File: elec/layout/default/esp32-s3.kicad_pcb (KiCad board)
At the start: 2 copper layers, 66.4 x 94.6 mm, 6 parts

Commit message: added layout
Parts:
- C1: value 100.0 nF -> Multilayer Ceramic Capacitors MLCC - SMD/SMT 100nF 10V 0402 RoHS
- C2, C3: value 10.0 uF -> Multilayer Ceramic Capacitors MLCC - SMD/SMT 10uF 10V 0805 RoHS
- R1: value 8.2 KΩ -> Chip Resistor - Surface Mount 11KOhms ±5% 1/16W 0402 RoHS
- moved C1 72.3 mm to (103.9, 82.7), turned to 90 degrees
- moved C2 71.2 mm to (102.4, 82.6), turned to 90 degrees
- moved R1 69.4 mm to (103.3, 85.4), turned to -90 degrees
- moved C3 68.7 mm to (100.4, 82.6), turned to 90 degrees
- moved U2 64.0 mm to (101.1, 87.4), turned to -90 degrees
- moved U1 45.9 mm to (114.4, 90.9)
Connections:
- net EN renamed en
- net IO0 renamed io0
- net IO1 renamed io1
- net IO10 renamed io10
- net IO11 renamed io11
- net IO12 renamed io12
- net IO13 renamed io13
- net IO14 renamed io14
- net IO15 renamed io15
- net IO16 renamed io16
- net IO17 renamed io17
- net IO18 renamed io18
- net IO2 renamed io2
- net IO21 renamed io21
- net IO3 renamed io3
- net IO35 renamed io35
- net IO36 renamed io36
- net IO37 renamed io37
- net IO38 renamed io38
- net IO4 renamed io4
- net IO45 renamed io45
- net IO46 renamed io46
- net IO47 renamed io47
- net IO48 renamed io48
- net IO5 renamed io5
- net IO6 renamed io6
- net IO7 renamed io7
- net IO8 renamed io8
- net IO9 renamed io9
- net RXD0 renamed rxd0
- net TXD0 renamed txd0
- net dm renamed io19
- net dp renamed io20
- net tck renamed io39
- net tdi renamed io41
- net tdo renamed io40
- net tms renamed io42
- C1 pad 1: vcc-1 -> vcc
- C1 pad 2: gnd-1 -> gnd
- C2 pad 1: vcc-2 -> vcc
- C2 pad 2: gnd-2 -> gnd
- C3 pad 1: vcc-3 -> vcc
- C3 pad 2: gnd-3 -> gnd
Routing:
- net en: track 0.00 -> 8.40 mm
- net vcc: track 0.00 -> 7.15 mm
- net gnd: track 0.00 -> 5.54 mm

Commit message: layout updates
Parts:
- C1: value Multilayer Ceramic Capacitors MLCC - SMD/SMT 100nF 10V 0402 RoHS -> 16V 100nF X7R ±10% 0402 Multilayer Ceramic Capacitors MLCC - SMD/SMT ROHS
- C2, C3: value Multilayer Ceramic Capacitors MLCC - SMD/SMT 10uF 10V 0805 RoHS -> 25V 10uF X5R ±10% 0805 Multilayer Ceramic Capacitors MLCC - SMD/SMT ROHS
- R1: value Chip Resistor - Surface Mount 11KOhms ±5% 1/16W 0402 RoHS -> 62.5mW Thick Film Resistors ±100ppm/℃ ±1% 10kΩ 0402 Chip Resistor - Surface Mount ROHS
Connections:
- net gnd renamed ic-gnd
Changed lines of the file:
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@@
   (net 30 "io39")
   (net 31 "io40")
-  (net 32 "gnd")
+  (net 32 "ic-gnd")
   (net 33 "vcc")
   (net 34 "io41")
@@
         (effects (font (size 1 1) (thickness 0.15)))
     )
-    (fp_text value "Multilayer Ceramic Capacitors MLCC - SMD/SMT 100nF 10V 0402 RoHS" (at 0 1.16 90) (layer "F.Fab")
+    (fp_text value "16V 100nF X7R ±10% 0402  Multilayer Ceramic Capacitors MLCC - SMD/SMT ROHS" (at 0 1.16 90) (layer "F.Fab")
         (effects (font (size 1 1) (thickness 0.15)))
     )
@@
       (net 33 "vcc") (pintype "stereo"))
     (pad "2" smd roundrect (at 0.48 0 90) (size 0.56 0.62) (layers "F.Cu" "F.Paste" "F.Mask") (roundrect_rratio 0.25)
-      (net 32 "gnd") (pintype "stereo"))
+      (net 32 "ic-gnd") (pintype "stereo"))
     (model "${KICAD6_3DMODEL_DIR}/Capacitor_SMD.3dshapes/C_0402_1005Metric.wrl"
       (offset (xyz 0 0 0))
@@
         (effects (font (size 1 1) (thickness 0.15)))
     )
-    (fp_text value "Multilayer Ceramic Capacitors MLCC - SMD/SMT 10uF 10V 0805 RoHS" (at 0 1.68 90) (layer "F.Fab")
+    (fp_text value "25V 10uF X5R ±10% 0805  Multilayer Ceramic Capacitors MLCC - SMD/SMT ROHS" (at 0 1.68 90) (layer "F.Fab")
         (effects (font (size 1 1) (thickness 0.15)))
     )
@@
       (net 33 "vcc") (pintype "stereo"))
     (pad "2" smd roundrect (at 0.95 0 90) (size 1 1.45) (layers "F.Cu" "F.Paste" "F.Mask") (roundrect_rratio 0.25)
-      (net 32 "gnd") (pintype "stereo"))
+      (net 32 "ic-gnd") (pintype "stereo"))
     (model "${KICAD6_3DMODEL_DIR}/Capacitor_SMD.3dshapes/C_0805_2012Metric.wrl"
       (offset (xyz 0 0 0))
-      (scale (xyz 1 1 1))
-      (rotate (xyz 0 0 0))
-    )
-  )
-  (footprint "lib:KEY-SMD_4P-L4.2-W3.2-P2.20-LS4.6" (layer "F.Cu")
-    (at 101.112894 87.388566 -90)
-    (attr smd)
-    (fp_text reference "U2" (at 1.943223 -2.508599 90) (layer "F.SilkS")
-        (effects (font (size 1 1) (thickness 0.15)))
-    )
-    (fp_text value "" (at 0 5.07 90) (layer "F.Fab")
-        (effects (font (size 1 1) (thickness 0.15)))
-    )
-    (fp_text user "${REFERENCE}" (at 0 0 90) (layer "F.Fab")
-        (effects (font (size 1 1) (thickness 0.15)))
-    )
-    (fp_line (start -2.2 -0.54) (end -2.2 0.54)
-      (stroke (width 0.25) (type solid)) (layer "F.SilkS"))
-    (fp_line (start -1.38 1.55) (end 1.38 1.55)
-      (stroke (width 0.25) (type solid)) (layer "F.SilkS"))
-    (fp_line (start -0.51 -1.02) (end 0.51 -1.02)
-      (stroke (width 0.25) (type solid)) (layer "F.SilkS"))
-    (fp_line (start -0.51 1.02) (end 0.51 1.02)
-      (stroke (width 0.25) (type solid)) (layer "F.SilkS"))
-    (fp_line (start 1.37 -1.52) (end -1.37 -1.52)
-      (stroke (width 0.25) (type solid)) (layer "F.SilkS"))
-    (fp_line (start 2.2 -0.54) (end 2.2 0.54)
-      (stroke (width 0.25) (type solid)) (layer "F.SilkS"))
-    (fp_arc (start -0.51 1.02) (mid -1.53 0) (end -0.51 -1.02)
-      (stroke (width 0.25) (type solid)) (layer "F.SilkS"))
-    (fp_arc (start 0.51 -1.02) (mid 1.53 0) (end 0.51 1.02)
-      (stroke (width 0.25) (type solid)) (layer "F.SilkS"))
-    (fp_circle (center -2.3 -1.6) (end -2.27 -1.6)
-      (stroke (width 0.06) (type solid)) (fill none) (layer "F.Fab"))
-    (pad "1" smd rect (at -2.1 -1.07 270) (size 1.05 0.7) (layers "F.Cu" "F.Paste" "F.Mask")
-      (net 1 "en") (pintype "stereo"))
-    (pad "2" smd rect (at 2.1 -1.07 270) (size 1.05 0.7) (layers "F.Cu" "F.Paste" "F.Mask")
-      (net 1 "en") (pintype "stereo"))
-    (pad "3" smd rect (at -2.1 1.07 270) (size 1.05 0.7) (layers "F.Cu" "F.Paste" "F.Mask")
-      (net 32 "gnd") (pintype "stereo"))
-    (pad "4" smd rect (at 2.1 1.07 270) (size 1.05 0.7) (layers "F.Cu" "F.Paste" "F.Mask")
-      (net 32 "gnd") (pintype "stereo"))
-    (model "/Users/narayanpowderly/Documents/atopile-workspace/blinky/.ato/modules/generics/elec/footprints/footprints.3dshapes/KEY-SMD_4P-L4.2-W3.2-H2.5-LS4.6-P2.2.wrl"
-      (offset (xyz 0 -0 -0))
       (scale (xyz 1 1 1))
       (rotate (xyz 0 0 0))
@@
         (effects (font (size 1 1) (thickness 0.15)))
     )
-    (fp_text value "Chip Resistor - Surface Mount 11KOhms ±5% 1/16W 0402 RoHS" (at 0 1.17 90) (layer "F.Fab")
+    (fp_text value "62.5mW Thick Film Resistors ±100ppm/℃ ±1% 10kΩ 0402  Chip Resistor - Surface Mount ROHS" (at 0 1.17 90) (layer "F.Fab")
         (effects (font (size 1 1) (thickness 0.15)))
     )
@@
     (pad "" thru_hole circle (at -0.1 -0.47) (size 0.5 0.5) (drill 0.3) (layers "*.Cu" "*.Paste" "*.Mask"))
     (pad "1" smd rect (at -8.75 -8.89) (size 1.5 0.9) (layers "F.Cu" "F.Paste" "F.Mask")
-      (net 32 "gnd") (pintype "stereo"))
+      (net 32 "ic-gnd") (pintype "stereo"))
     (pad "2" smd rect (at -8.75 -7.62) (size 1.5 0.9) (layers "F.Cu" "F.Paste" "F.Mask")
       (net 33 "vcc") (pintype "stereo"))
@@
       (net 39 "io1") (pintype "stereo"))
     (pad "40" smd rect (at 8.75 -8.89 180) (size 1.5 0.9) (layers "F.Cu" "F.Paste" "F.Mask")
-      (net 32 "gnd") (pintype "stereo"))
+      (net 32 "ic-gnd") (pintype "stereo"))
     (pad "41" smd rect (at -2.9 -2.57 90) (size 0.9 0.9) (layers "F.Cu" "F.Paste" "F.Mask")
-      (net 32 "gnd") (pintype "stereo"))
+      (net 32 "ic-gnd") (pintype "stereo"))
     (pad "41" smd rect (at -2.9 -1.17 90) (size 0.9 0.9) (layers "F.Cu" "F.Paste" "F.Mask")
-      (net 32 "gnd") (pintype "stereo"))
+      (net 32 "ic-gnd") (pintype "stereo"))
     (pad "41" smd rect (at -2.9 0.23 90) (size 0.9 0.9) (layers "F.Cu" "F.Paste" "F.Mask")
-      (net 32 "gnd") (pintype "stereo"))
+      (net 32 "ic-gnd") (pintype "stereo"))
     (pad "41" smd rect (at -1.5 -2.57 90) (size 0.9 0.9) (layers "F.Cu" "F.Paste" "F.Mask")
-      (net 32 "gnd") (pintype "stereo"))
+      (net 32 "ic-gnd") (pintype "stereo"))
     (pad "41" smd rect (at -1.5 -1.17 90) (size 0.9 0.9) (layers "F.Cu" "F.Paste" "F.Mask")
-      (net 32 "gnd") (pintype "stereo"))
+      (net 32 "ic-gnd") (pintype "stereo"))
     (pad "41" smd rect (at -1.5 0.23 90) (size 0.9 0.9) (layers "F.Cu" "F.Paste" "F.Mask")
-      (net 32 "gnd") (pintype "stereo"))
+      (net 32 "ic-gnd") (pintype "stereo"))
     (pad "41" smd rect (at -0.1 -2.57 90) (size 0.9 0.9) (layers "F.Cu" "F.Paste" "F.Mask")
-      (net 32 "gnd") (pintype "stereo"))
+      (net 32 "ic-gnd") (pintype "stereo"))
     (pad "41" smd rect (at -0.1 -1.17 90) (size 0.9 0.9) (layers "F.Cu" "F.Paste" "F.Mask")
-      (net 32 "gnd") (pintype "stereo"))
+      (net 32 "ic-gnd") (pintype "stereo"))
     (pad "41" smd rect (at -0.1 0.23 90) (size 0.9 0.9) (layers "F.Cu" "F.Paste" "F.Mask")
-      (net 32 "gnd") (pintype "stereo"))
+      (net 32 "ic-gnd") (pintype "stereo"))
     (model "/Users/narayanpowderly/Documents/atopile-workspace/packages/esp32-s3/elec/footprints/footprints.3dshapes/WIRELM-SMD_ESP32-S3-WROOM-1.wrl"
       (offset (xyz 0 3.65 -0))
+      (scale (xyz 1 1 1))
+      (rotate (xyz 0 0 0))
+    )
+  )
+  (footprint "lib:KEY-SMD_4P-L4.2-W3.2-P2.20-LS4.6" (layer "F.Cu")
+    (at 101.123843 87.39919 -90)
+    (attr smd)
+    (fp_text reference "U2" (at 0 -5.07 90) (layer "F.SilkS")
+        (effects (font (size 1 1) (thickness 0.15)))
+    )
+    (fp_text value "" (at 0 5.07 90) (layer "F.Fab")
+        (effects (font (size 1 1) (thickness 0.15)))
+    )
+    (fp_text user "${REFERENCE}" (at 0 0 90) (layer "F.Fab")
+        (effects (font (size 1 1) (thickness 0.15)))
+    )
+    (fp_line (start -2.2 -0.54) (end -2.2 0.54)
+      (stroke (width 0.25) (type solid)) (layer "F.SilkS"))
+    (fp_line (start -1.38 1.55) (end 1.38 1.55)
+      (stroke (width 0.25) (type solid)) (layer "F.SilkS"))
+    (fp_line (start -0.51 -1.02) (end 0.51 -1.02)
+      (stroke (width 0.25) (type solid)) (layer "F.SilkS"))
+    (fp_line (start -0.51 1.02) (end 0.51 1.02)
+      (stroke (width 0.25) (type solid)) (layer "F.SilkS"))
+    (fp_line (start 1.37 -1.52) (end -1.37 -1.52)
+      (stroke (width 0.25) (type solid)) (layer "F.SilkS"))
+    (fp_line (start 2.2 -0.54) (end 2.2 0.54)
+      (stroke (width 0.25) (type solid)) (layer "F.SilkS"))
+    (fp_arc (start -0.51 1.02) (mid -1.53 0) (end -0.51 -1.02)
+      (stroke (width 0.25) (type solid)) (layer "F.SilkS"))
+    (fp_arc (start 0.51 -1.02) (mid 1.53 0) (end 0.51 1.02)
+      (stroke (width 0.25) (type solid)) (layer "F.SilkS"))
+    (fp_circle (center -2.3 -1.6) (end -2.27 -1.6)
+      (stroke (width 0.06) (type solid)) (fill none) (layer "F.Fab"))
+    (pad "1" smd rect (at -2.1 -1.07 270) (size 1.05 0.7) (layers "F.Cu" "F.Paste" "F.Mask")
+      (net 1 "en") (pintype "stereo"))
+    (pad "2" smd rect (at 2.1 -1.07 270) (size 1.05 0.7) (layers "F.Cu" "F.Paste" "F.Mask")
+      (net 1 "en") (pintype "stereo"))
+    (pad "3" smd rect (at -2.1 1.07 270) (size 1.05 0.7) (layers "F.Cu" "F.Paste" "F.Mask")
+      (net 32 "ic-gnd") (pintype "stereo"))
+    (pad "4" smd rect (at 2.1 1.07 270) (size 1.05 0.7) (layers "F.Cu" "F.Paste" "F.Mask")
+      (net 32 "ic-gnd") (pintype "stereo"))
+    (model "/Users/narayanpowderly/Documents/atopile-workspace/blinky/.ato/modules/generics/elec/footprints/footprints.3dshapes/KEY-SMD_4P-L4.2-W3.2-H2.5-LS4.6-P2.2.wrl"
+      (offset (xyz 0 -0 -0))
       (scale (xyz 1 1 1))
       (rotate (xyz 0 0 0))
@@
         (effects (font (size 1 1) (thickness 0.15)))
     )
-    (fp_text value "Multilayer Ceramic Capacitors MLCC - SMD/SMT 10uF 10V 0805 RoHS" (at 0 1.68 90) (layer "F.Fab")
+    (fp_text value "25V 10uF X5R ±10% 0805  Multilayer Ceramic Capacitors MLCC - SMD/SMT ROHS" (at 0 1.68 90) (layer "F.Fab")
         (effects (font (size 1 1) (thickness 0.15)))
     )
@@
       (net 33 "vcc") (pintype "stereo"))
     (pad "2" smd roundrect (at 0.95 0 90) (size 1 1.45) (layers "F.Cu" "F.Paste" "F.Mask") (roundrect_rratio 0.25)
-      (net 32 "gnd") (pintype "stereo"))
+      (net 32 "ic-gnd") (pintype "stereo"))
     (model "${KICAD6_3DMODEL_DIR}/Capacitor_SMD.3dshapes/C_0805_2012Metric.wrl"
       (offset (xyz 0 0 0))

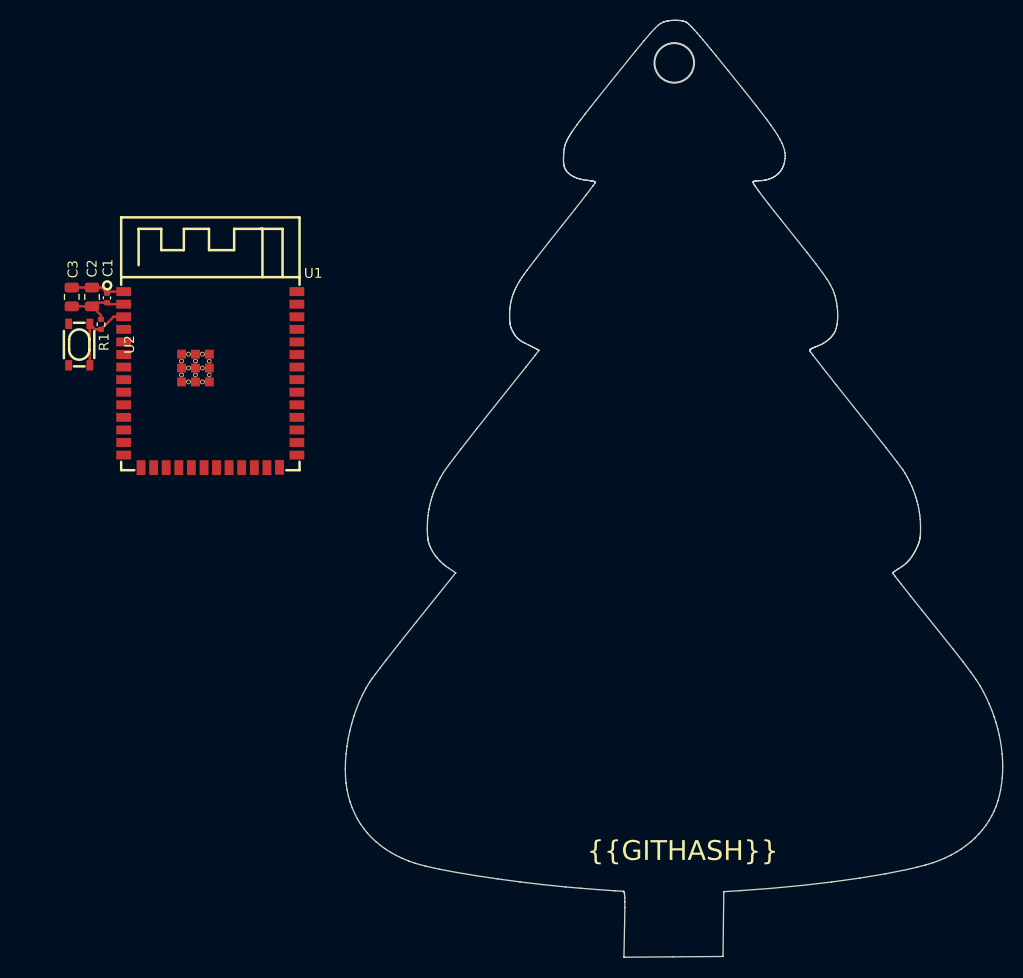
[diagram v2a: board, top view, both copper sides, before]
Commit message: Remove xmas tree from layout
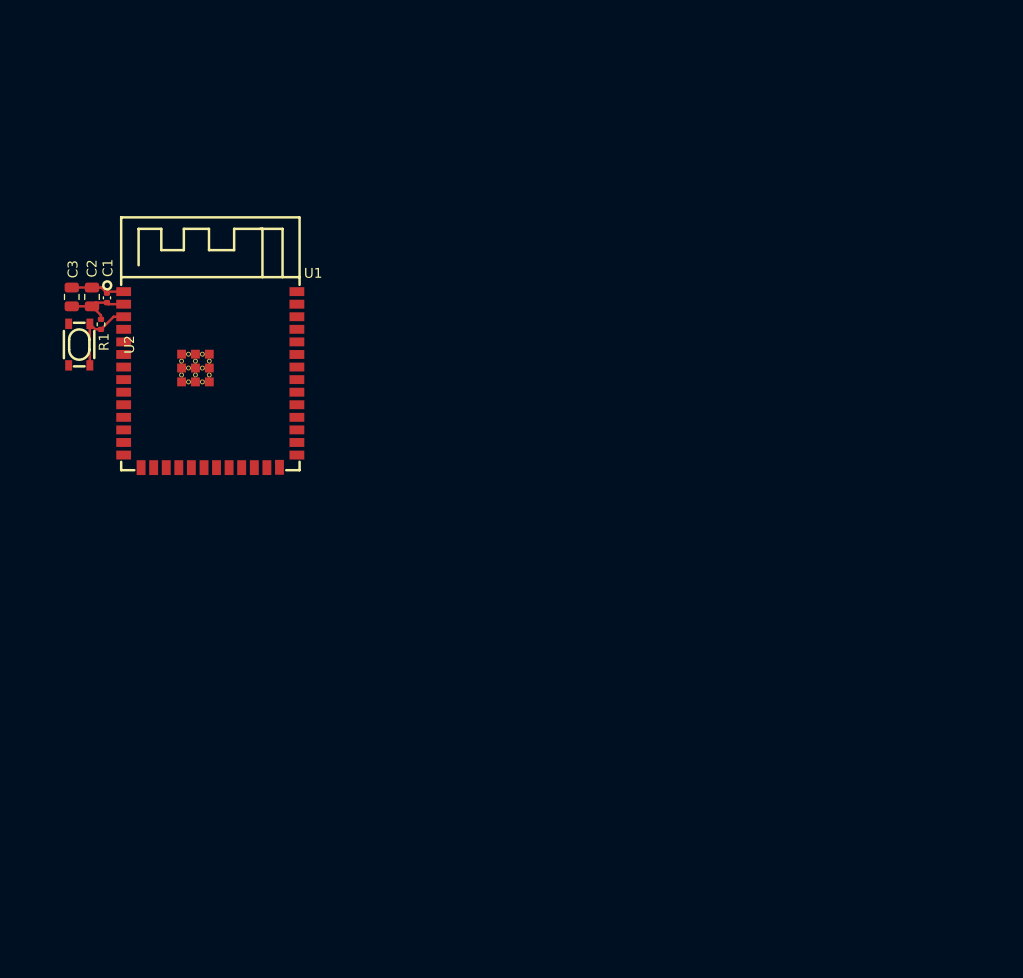
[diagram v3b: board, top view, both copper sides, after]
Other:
- board outline removed
- board text removed: "{{GITHASH}}"

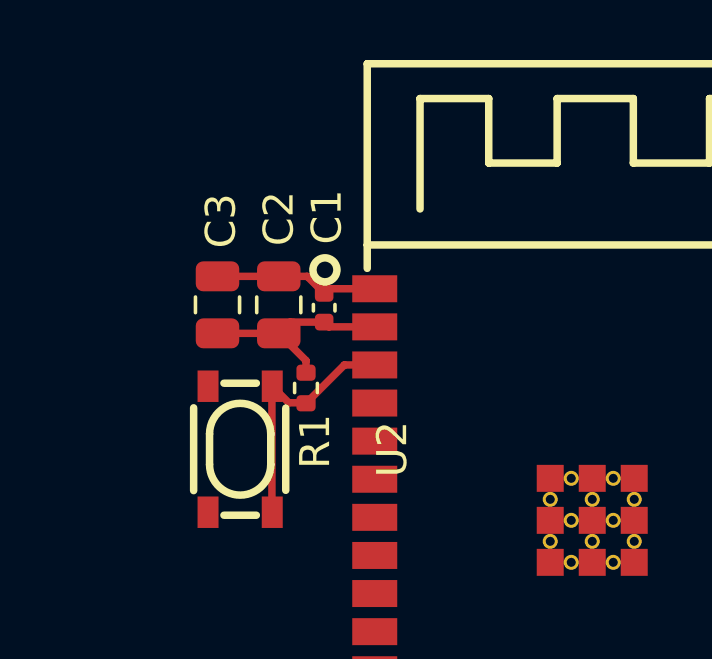
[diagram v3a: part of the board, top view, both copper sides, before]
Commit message: run build with 0.3 compiler
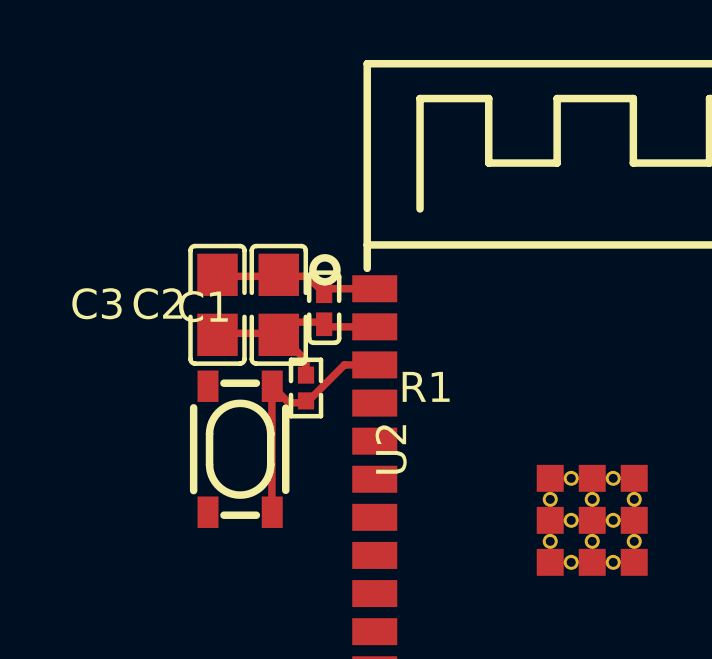
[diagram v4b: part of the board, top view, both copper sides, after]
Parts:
- C1: value 16V 100nF X7R ±10% 0402 Multilayer Ceramic Capacitors MLCC - SMD/SMT ROHS -> 100nF ±10% 16V X7R; footprint lib:C0402 -> atopile:C0402-b3ef17
- C2, C3: value 25V 10uF X5R ±10% 0805 Multilayer Ceramic Capacitors MLCC - SMD/SMT ROHS -> 10µF ±10% 25V X5R; footprint lib:C0805 -> atopile:C0805-3b2e55
- R1: value 62.5mW Thick Film Resistors ±100ppm/℃ ±1% 10kΩ 0402 Chip Resistor - Surface Mount ROHS -> 10kΩ ±1% 62.5mW; footprint lib:R0402 -> atopile:R0402-56259e
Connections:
- net en renamed in
- net ic-gnd renamed gnd
- net io10 renamed cs
- net io11 renamed mosi
- net io12 renamed sck
- net io13 renamed miso
- net io19 renamed dm
- net io20 renamed dp
- net io39 renamed tck
- net io40 renamed tdo
- net io41 renamed tdi
- net io42 renamed tms
- net io6 renamed scl
- net io7 renamed sda
- net rxd0 renamed RXD0
- net txd0 renamed TXD0
- net vcc renamed hv

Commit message: Revert "run build with 0.3 compiler"
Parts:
- C1: value 100nF ±10% 16V X7R -> 16V 100nF X7R ±10% 0402 Multilayer Ceramic Capacitors MLCC - SMD/SMT ROHS; footprint atopile:C0402-b3ef17 -> lib:C0402
- C2, C3: value 10µF ±10% 25V X5R -> 25V 10uF X5R ±10% 0805 Multilayer Ceramic Capacitors MLCC - SMD/SMT ROHS; footprint atopile:C0805-3b2e55 -> lib:C0805
- R1: value 10kΩ ±1% 62.5mW -> 62.5mW Thick Film Resistors ±100ppm/℃ ±1% 10kΩ 0402 Chip Resistor - Surface Mount ROHS; footprint atopile:R0402-56259e -> lib:R0402
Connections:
- net RXD0 renamed rxd0
- net TXD0 renamed txd0
- net cs renamed io10
- net dm renamed io19
- net dp renamed io20
- net gnd renamed ic-gnd
- net hv renamed vcc
- net in renamed en
- net miso renamed io13
- net mosi renamed io11
- net sck renamed io12
- net scl renamed io6
- net sda renamed io7
- net tck renamed io39
- net tdi renamed io41
- net tdo renamed io40
- net tms renamed io42

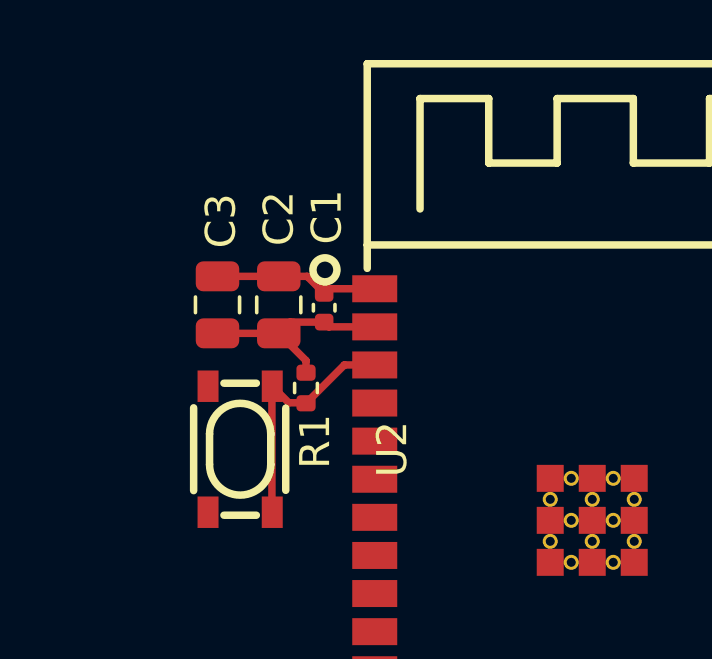
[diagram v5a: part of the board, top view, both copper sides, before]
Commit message: Update to build with the v0.3 compiler
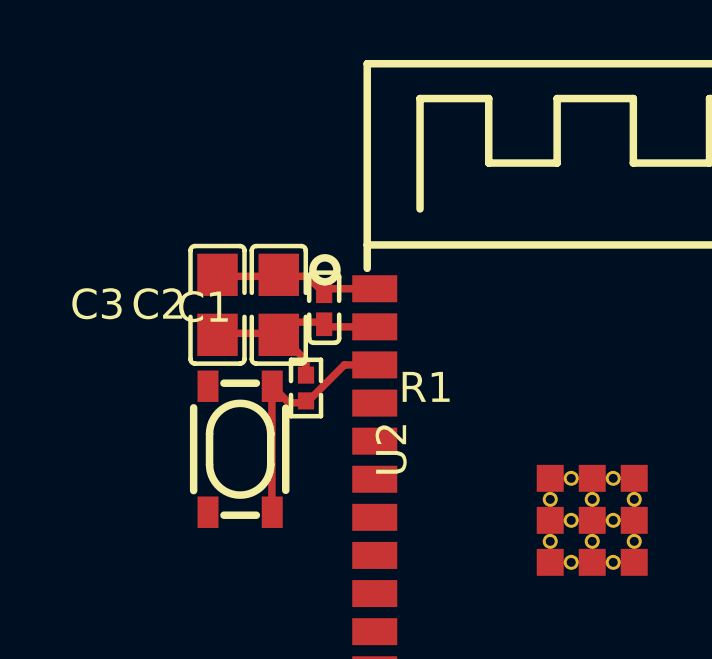
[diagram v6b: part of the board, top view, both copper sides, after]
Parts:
- C1: value 16V 100nF X7R ±10% 0402 Multilayer Ceramic Capacitors MLCC - SMD/SMT ROHS -> 100nF ±10% 16V X7R; footprint lib:C0402 -> atopile:C0402-b3ef17
- C2, C3: value 25V 10uF X5R ±10% 0805 Multilayer Ceramic Capacitors MLCC - SMD/SMT ROHS -> 10µF ±10% 25V X5R; footprint lib:C0805 -> atopile:C0805-3b2e55
- R1: value 62.5mW Thick Film Resistors ±100ppm/℃ ±1% 10kΩ 0402 Chip Resistor - Surface Mount ROHS -> 10kΩ ±1% 62.5mW; footprint lib:R0402 -> atopile:R0402-56259e
